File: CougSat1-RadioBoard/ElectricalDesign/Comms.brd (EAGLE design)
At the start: 90.4 x 95.8 mm, 317 parts, among them J1 700mm Antenna, J2 CougSat Card, J3 SWD, Q1 DMN53D0LDW, Q2 DMN53D0LDW, Q3 DMN53D0LDW, Q4 CSD25402Q3A, U1 AD8515, U10 AD8515, U11 AD8515, U12 TXS0102DQM, U13 ADF4360, U14 MAAM-011229, U15 INA199C2, U16 AD8515, U17 AD8515, U18 LP5907MFX-3.1, U19 HMC545A, U2 AD8515, U20 INA199C1, U21 TPS61236, U22 AD8345, U23 AD9761, U24 TXS0102DQM, U25 TXS0102DQM, U26 TXS0102DQM, U27 MMZ09332B, U28 AD8515, U29 ADF4360, U3 AD7291, U30 TXS0102DQM, U31 INA199C2, U32 TXS0102DQM, U33 LP5907MFX-3.1, U34 MAAM-011229, U35 TXS0102DQM, U36 TXS0102DQM, U37 STM32L496VGT, U38 IS25LP016D, U39 IS25LP016D, U4 AD7291, U5 MAAM-011229, U6 AD8348, U7 AD7291, U8 MAAM-011229, U9 TXS0102DQM, Y1 19.68MHz ±2.5ppm, Y2 19.68MHz ±2.5ppm, Y3 8MHz ±10ppm, Y4 32.768kHz ±10ppm

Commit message: Adjusted layout
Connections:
- net SELFNET renamed PA_HEATSINK
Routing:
- net PA_HEATSINK: track 0.00 -> 4.53 mm, vias 0 -> 7
- net DGND: track 2435.8 -> 2435.7 mm, vias 949 -> 944
- added copper zone on layer 15, net PA_HEATSINK
- added copper zone on layer 16, net PA_HEATSINK
- added copper zone on layer 2, net PA_HEATSINK
- removed copper zone on layer 16, net HEAT1
- removed copper zone on layer 15, net HEAT2
- removed copper zone on layer 2, net HEAT3
- removed copper zone on layer 1, net HEAT4
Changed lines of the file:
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@@
 <drawing>
 <settings>
-<setting alwaysvectorfont="no"/>
+<setting alwaysvectorfont="yes"/>
 <setting verticaltext="up"/>
 </settings>
@@
 <layer number="28" name="bValues" color="7" fill="1" visible="no" active="yes"/>
 <layer number="29" name="tStop" color="7" fill="3" visible="no" active="yes"/>
-<layer number="30" name="bStop" color="7" fill="6" visible="no" active="yes"/>
+<layer number="30" name="bStop" color="7" fill="6" visible="yes" active="yes"/>
 <layer number="31" name="tCream" color="7" fill="4" visible="no" active="yes"/>
 <layer number="32" name="bCream" color="7" fill="5" visible="no" active="yes"/>
@@
 <circle x="76.25" y="4.9" radius="0.3" width="0" layer="30"/>
 <circle x="76.25" y="3.5" radius="0.3" width="0" layer="30"/>
-<circle x="77.9" y="-3.4" radius="0.3" width="0" layer="30"/>
-<circle x="77.4" y="-2.9" radius="0.3" width="0" layer="30"/>
-<circle x="78.4" y="-2.9" radius="0.3" width="0" layer="30"/>
-<circle x="78.4" y="-3.9" radius="0.3" width="0" layer="30"/>
-<circle x="77.4" y="-3.9" radius="0.3" width="0" layer="30"/>
 <circle x="80" y="-3.4" radius="0.3" width="0" layer="30"/>
 <circle x="80" y="-4" radius="0.3" width="0" layer="30"/>
@@
 <circle x="78.7" y="0" radius="0.3" width="0" layer="30"/>
 <circle x="77.25" y="0.4" radius="0.3" width="0" layer="30"/>
-<circle x="76.5" y="-1.9" radius="0.3" width="0" layer="30"/>
 <circle x="79.3" y="-1.9" radius="0.3" width="0" layer="30"/>
 <circle x="79" y="2" radius="0.3" width="0" layer="30"/>
@@
 <circle x="37.6" y="34.85" radius="0.3" width="0" layer="30"/>
 <circle x="31.22" y="32.55" radius="0.3" width="0" layer="30"/>
+<polygon width="0.2" layer="30">
+<vertex x="76.1" y="-3.1"/>
+<vertex x="76.1" y="-1.5"/>
+<vertex x="76.2" y="-1.4"/>
+<vertex x="78.1" y="-1.4"/>
+<vertex x="79.4" y="-2.7"/>
+<vertex x="79.4" y="-4.2"/>
+<vertex x="77.2" y="-4.2"/>
+</polygon>
 </plain>
 <attributes>
@@
 <via x="76.25" y="4.9" extent="1-16" drill="0.3"/>
 <via x="76.25" y="3.5" extent="1-16" drill="0.3"/>
-<via x="77.9" y="-3.4" extent="1-16" drill="0.3"/>
-<via x="77.4" y="-2.9" extent="1-16" drill="0.3"/>
-<via x="78.4" y="-2.9" extent="1-16" drill="0.3"/>
-<via x="78.4" y="-3.9" extent="1-16" drill="0.3"/>
-<via x="77.4" y="-3.9" extent="1-16" drill="0.3"/>
 <via x="80" y="-3.4" extent="1-16" drill="0.3"/>
 <via x="80" y="-4" extent="1-16" drill="0.3"/>
@@
 </polygon>
 <polygon width="0.2" layer="15" thermals="no">
-<vertex x="77.3" y="-2.7"/>
-<vertex x="77.2" y="-2.8"/>
-<vertex x="77.2" y="-4"/>
-<vertex x="77.3" y="-4.1"/>
-<vertex x="78.5" y="-4.1"/>
-<vertex x="78.6" y="-4"/>
-<vertex x="78.6" y="-2.8"/>
-<vertex x="78.5" y="-2.7"/>
-</polygon>
-<polygon width="0.2" layer="15" thermals="no">
 <vertex x="79.9" y="-3.2"/>
 <vertex x="79.8" y="-3.3"/>
@@
 <wire x1="71" y1="1" x2="73.1" y2="-1.1" width="0.25" layer="2"/>
 <wire x1="73.1" y1="-1.1" x2="73.1" y2="-1.25" width="0.25" layer="2"/>
-<wire x1="79.3" y1="-2" x2="79.3" y2="-1.9" width="0.25" layer="2"/>
 <wire x1="80" y1="-3.4" x2="80" y2="-2.6" width="0.25" layer="2"/>
 <wire x1="80" y1="-2.6" x2="79.3" y2="-1.9" width="0.25" layer="2"/>
@@
 <wire x1="87.4" y1="-26.975" x2="40.175" y2="-26.975" width="0.16" layer="1"/>
 </signal>
-<signal name="SELFNET">
-<contactref element="U27" pad="PAD"/>
-</signal>
-<signal name="HEAT1">
-<polygon width="0.1524" layer="16">
-<vertex x="77.4" y="-3.8"/>
-<vertex x="76.9" y="-4.3"/>
-<vertex x="74.4" y="-4.3"/>
-<vertex x="75.1" y="-3.6"/>
-<vertex x="75.1" y="-2.2"/>
-<vertex x="76.7" y="-3.8"/>
-</polygon>
-</signal>
-<signal name="HEAT2">
-<polygon width="0.1524" layer="15">
-<vertex x="77.3" y="-2.9"/>
-<vertex x="74.5" y="-2.9"/>
-<vertex x="74.4" y="-3"/>
-<vertex x="74.4" y="-1.1"/>
-<vertex x="75.5" y="0"/>
-<vertex x="76.7" y="0"/>
-<vertex x="77.3" y="-0.6"/>
-</polygon>
-</signal>
-<signal name="HEAT4">
-<polygon width="0.1524" layer="1">
-<vertex x="78.5" y="-3.9"/>
-<vertex x="76" y="-6.4"/>
-<vertex x="76" y="-6.6"/>
-<vertex x="77.2" y="-7.8"/>
-<vertex x="79.5" y="-7.8"/>
-<vertex x="81.3" y="-7.8"/>
-<vertex x="81.8" y="-7.3"/>
-<vertex x="78.5" y="-4"/>
-</polygon>
-</signal>
-<signal name="HEAT3">
-<polygon width="0.1524" layer="2">
-<vertex x="78.4" y="-2.9"/>
-<vertex x="76.9" y="-1.4"/>
+<signal name="PA_HEATSINK">
+<polygon width="0.2" layer="2">
+<vertex x="78.6" y="-4.1"/>
+<vertex x="77.2" y="-4.1"/>
+<vertex x="77.2" y="-2.7"/>
+<vertex x="78.6" y="-2.7"/>
+</polygon>
+<polygon width="0.2" layer="15">
+<vertex x="79" y="-4.9"/>
+<vertex x="76.8" y="-4.9"/>
+<vertex x="75.9" y="-4"/>
+<vertex x="75.9" y="-1.7"/>
 <vertex x="76.2" y="-1.4"/>
-<vertex x="77.7" y="0.1"/>
-<vertex x="78" y="0.1"/>
-<vertex x="79.6" y="-1.5"/>
-<vertex x="79.6" y="-2.9"/>
+<vertex x="78.5" y="-1.4"/>
+<vertex x="79.4" y="-2.3"/>
+<vertex x="79.4" y="-4.5"/>
+</polygon>
+<polygon width="0.2" layer="16">
+<vertex x="79.4" y="-4.5"/>
+<vertex x="77.1" y="-4.5"/>
+<vertex x="75.9" y="-3.3"/>
+<vertex x="75.9" y="-1.7"/>
+<vertex x="76.2" y="-1.4"/>
+<vertex x="79.5" y="-1.4"/>
+<vertex x="79.8" y="-1.7"/>
+<vertex x="79.8" y="-4.1"/>
 </polygon>
+<contactref element="U27" pad="PAD"/>
+<via x="77.9" y="-3.4" extent="1-16" drill="0.3"/>
+<via x="78.4" y="-2.9" extent="1-16" drill="0.3"/>
+<via x="78.4" y="-3.9" extent="1-16" drill="0.3"/>
+<via x="77.4" y="-3.9" extent="1-16" drill="0.3"/>
+<via x="77.4" y="-2.9" extent="1-16" drill="0.3"/>
+<via x="76.7" y="-2.2" extent="1-16" drill="0.3"/>
+<via x="76.2" y="-1.7" extent="1-16" drill="0.3"/>
+<wire x1="76.2" y1="-1.7" x2="76.7" y2="-2.2" width="0.2" layer="15"/>
+<wire x1="76.7" y1="-2.2" x2="77.4" y2="-2.9" width="0.2" layer="15"/>
+<wire x1="77.4" y1="-2.9" x2="77.9" y2="-3.4" width="0.2" layer="15"/>
+<wire x1="77.9" y1="-3.4" x2="78.4" y2="-3.9" width="0.2" layer="15"/>
+<wire x1="78.4" y1="-2.9" x2="77.9" y2="-3.4" width="0.2" layer="15"/>
+<wire x1="77.4" y1="-3.9" x2="77.9" y2="-3.4" width="0.2" layer="15"/>
 </signal>
 </signals>

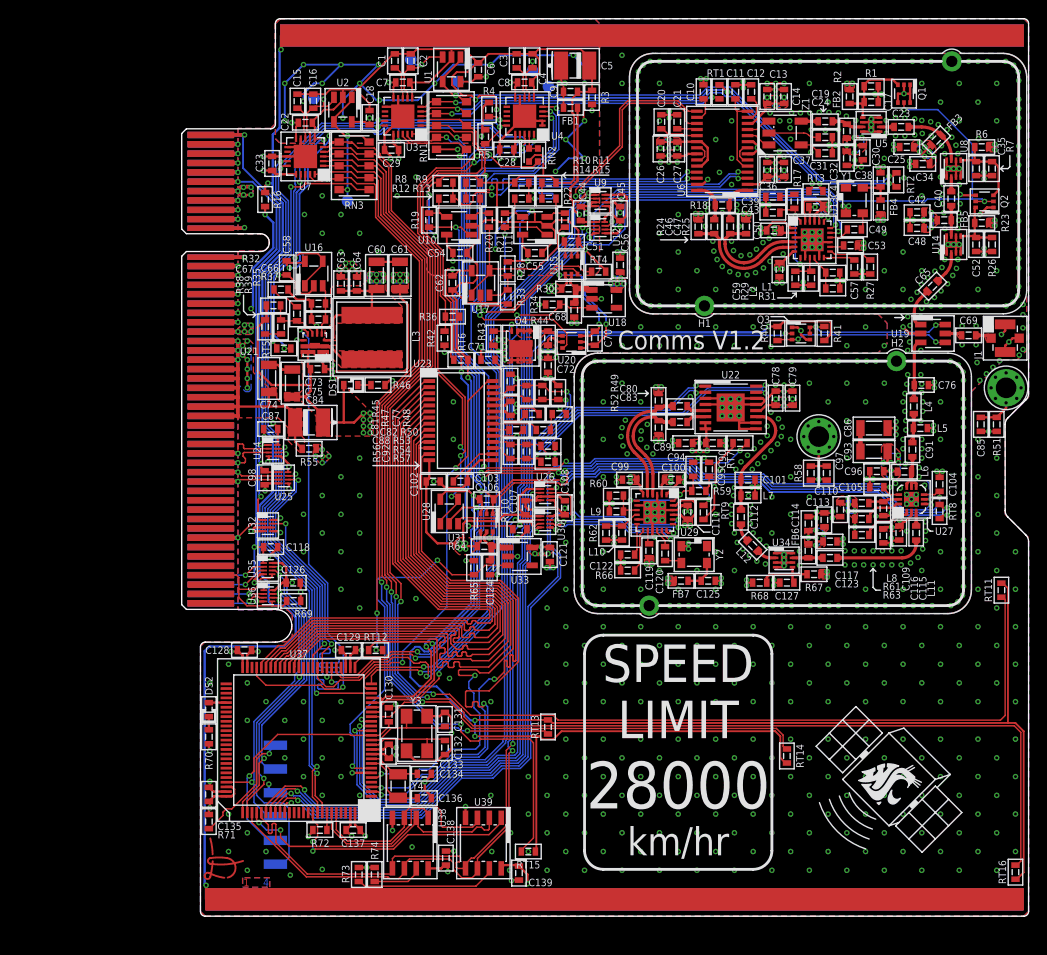
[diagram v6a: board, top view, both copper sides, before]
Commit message: Added nFET
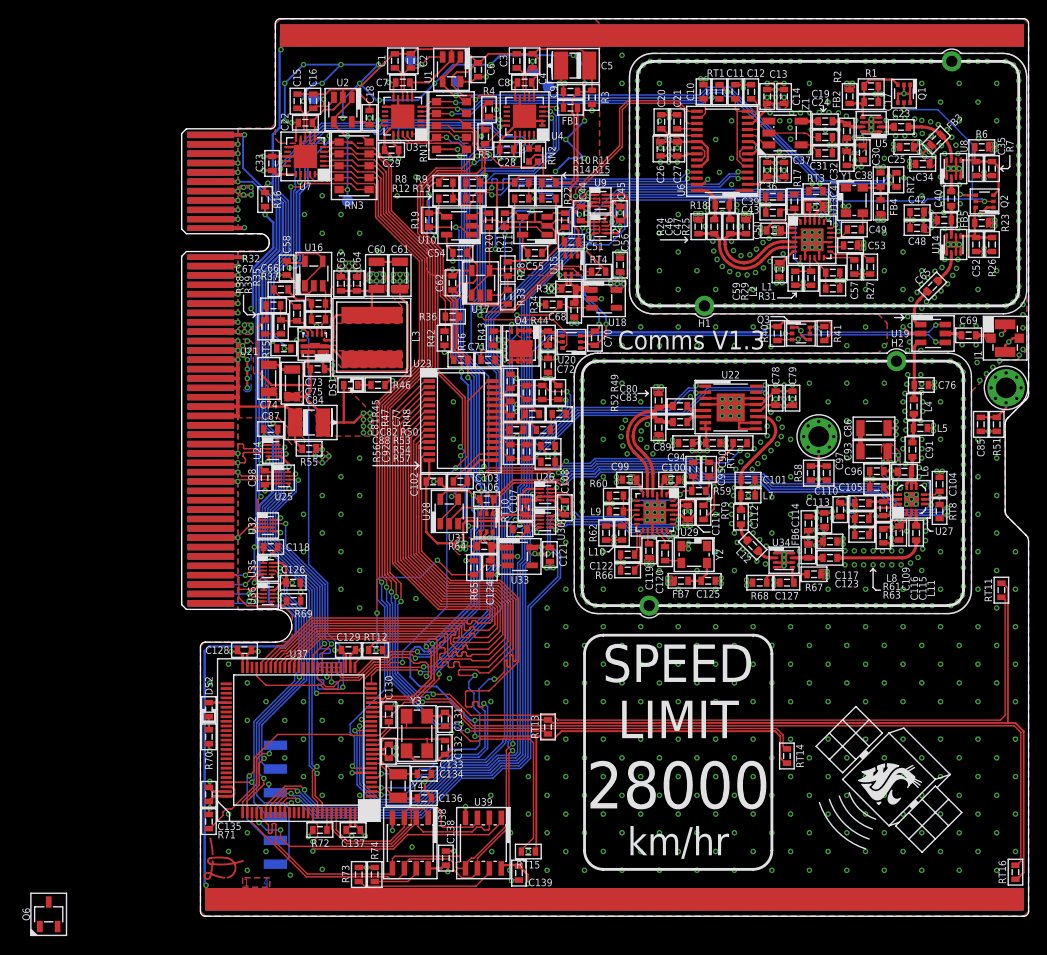
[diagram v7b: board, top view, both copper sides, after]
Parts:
- added Q6: DMN53D0L, CougsInSpace-DiscreteSemi:SOT23-3
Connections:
- new net PC_5.0: Q6.1
- net !PC_5.0V-1: now also Q6.3
- net PGND: now also Q6.2
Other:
- board text added: "Comms V1.3"
- board text removed: "Comms V1.2"
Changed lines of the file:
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@@
 <drawing>
 <settings>
-<setting alwaysvectorfont="yes"/>
+<setting alwaysvectorfont="no"/>
 <setting verticaltext="up"/>
 </settings>
@@
 <wire x1="77.1" y1="16" x2="76.8" y2="16.3" width="0.15" layer="21"/>
 <wire x1="77.1" y1="16" x2="76.8" y2="15.7" width="0.15" layer="21"/>
-<text x="54.4" y="13.6" size="2" layer="21" font="vector" ratio="15" align="center">Comms V1.2</text>
+<text x="54.4" y="13.6" size="2" layer="21" font="vector" ratio="15" align="center">Comms V1.3</text>
 <text x="6.9" y="-44.3" size="0.8" layer="1" font="vector" ratio="15" align="center">1</text>
 <text x="7.6" y="-44.3" size="0.8" layer="2" font="vector" ratio="15" align="center">2</text>
@@
 <attribute name="TEMP" value="25ppm/°C" x="6.1" y="-28.25" size="0.8" layer="27" ratio="15" rot="R90" display="off"/>
 </element>
+<element name="Q6" library="CougsInSpace-DiscreteSemi" package="SOT23-3" value="DMN53D0L" x="-14.2" y="-47.7" smashed="yes" rot="R90">
+<attribute name="CURRENT" value="500mA" x="-14.2" y="-47.7" size="1.778" layer="27" rot="R90" display="off"/>
+<attribute name="NAME" x="-16.6" y="-47.7" size="0.8" layer="25" font="vector" ratio="15" rot="R90" align="center"/>
+<attribute name="RDS" value="4.5mΩ" x="-14.2" y="-47.7" size="1.778" layer="27" rot="R90" display="off"/>
+<attribute name="SKU" value="56-0003" x="-14.2" y="-47.7" size="1.778" layer="27" rot="R90" display="off"/>
+<attribute name="VDS" value="50V" x="-14.2" y="-47.7" size="1.778" layer="27" rot="R90" display="off"/>
+</element>
 </elements>
 <signals>
@@
 <wire x1="23.3" y1="18.2" x2="24.15" y2="17.35" width="0.25" layer="1"/>
 <wire x1="24.15" y1="17.35" x2="24.15" y2="10.65" width="0.25" layer="1"/>
+<contactref element="Q6" pad="2"/>
+<wire x1="3.1" y1="5.5" x2="-13.25" y2="-49.01" width="0" layer="19" extent="1-1"/>
 </signal>
 <signal name="CHASSIS" class="3">
@@
 <wire x1="20.25" y1="-27.1" x2="19.4" y2="-27.1" width="0.16" layer="1"/>
 <wire x1="19.4" y1="-27.1" x2="19.2" y2="-26.9" width="0.16" layer="1"/>
+<contactref element="Q6" pad="3"/>
+<wire x1="19.2" y1="-26.9" x2="-14.2" y2="-46.39" width="0" layer="19" extent="1-1"/>
 </signal>
 <signal name="I_5.0V-1">
@@
 <wire x1="77.4" y1="-3.9" x2="77.9" y2="-3.4" width="0.2" layer="15"/>
 </signal>
+<signal name="PC_5.0">
+<contactref element="Q6" pad="1"/>
+</signal>
 </signals>

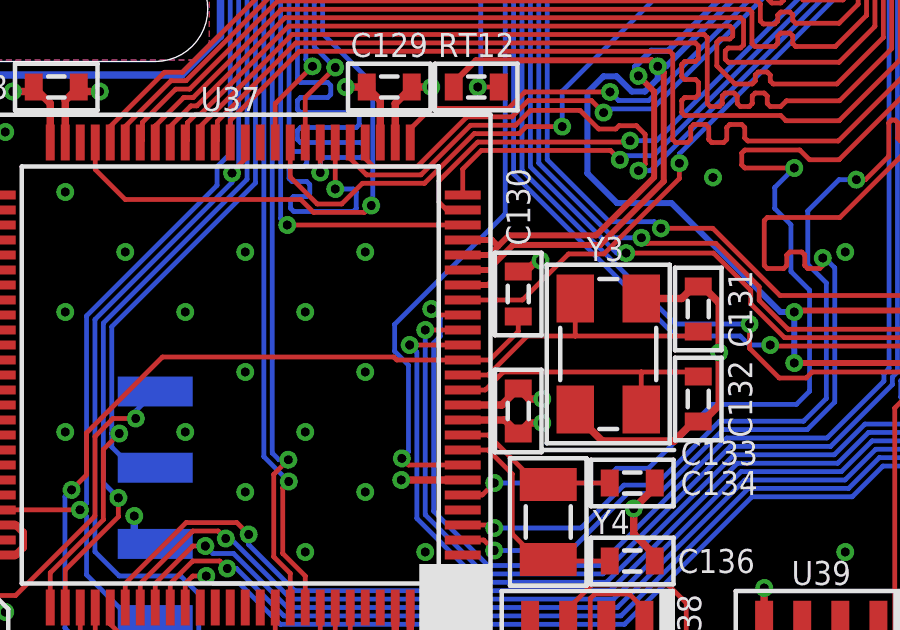
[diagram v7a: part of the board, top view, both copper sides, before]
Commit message: Fixed net names
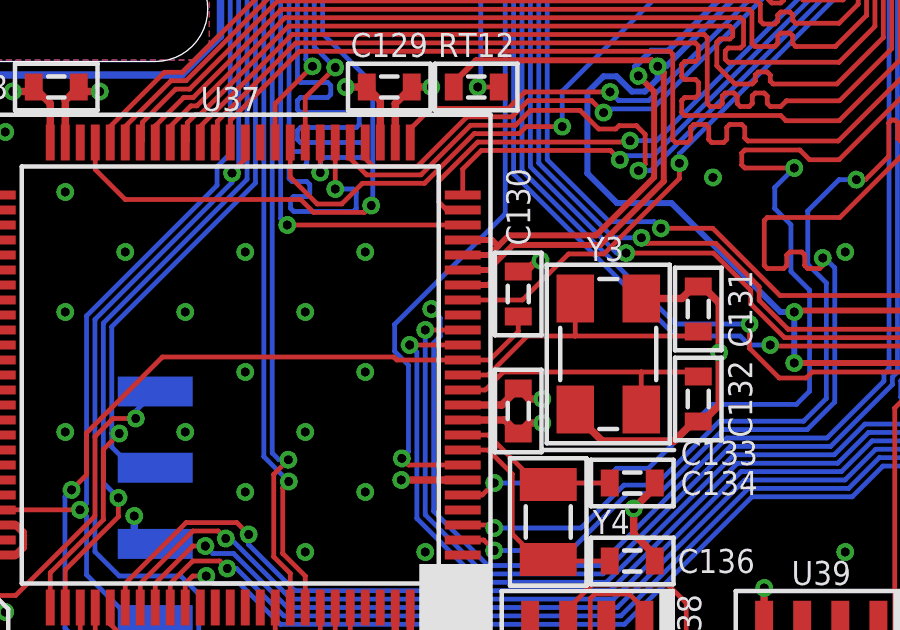
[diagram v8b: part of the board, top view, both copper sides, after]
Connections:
- removed net !PC_5.0V-1: Q4.4, Q6.3, R43.1, U37.17
- removed net PC_5.0: Q6.1
- new net !PC_5.0V: Q4.4, Q6.3, R43.1
- new net PC_5.0V: Q6.1, U37.17
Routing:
- net !PC_5.0V-1: track 74.0 -> 0.00 mm, vias 2 -> 0
- net !PC_5.0V: track 0.00 -> 73.1 mm, vias 0 -> 2
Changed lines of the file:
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@@
 <wire x1="21.13" y1="-11.74" x2="25.46" y2="-11.74" width="0.16" layer="16"/>
 </signal>
-<signal name="!PC_5.0V-1">
+<signal name="!PC_5.0V">
 <contactref element="Q4" pad="4"/>
 <contactref element="R43" pad="1"/>
@@
 <wire x1="19.28" y1="-28.03" x2="19.5" y2="-27.81" width="0.16" layer="16"/>
 <wire x1="19.5" y1="-27.81" x2="19.5" y2="-27.2" width="0.16" layer="16"/>
-<contactref element="U37" pad="17"/>
-<wire x1="20.25" y1="-27.1" x2="19.4" y2="-27.1" width="0.16" layer="1"/>
 <wire x1="19.4" y1="-27.1" x2="19.2" y2="-26.9" width="0.16" layer="1"/>
 <contactref element="Q6" pad="3"/>
@@
 <wire x1="77.4" y1="-3.9" x2="77.9" y2="-3.4" width="0.2" layer="15"/>
 </signal>
-<signal name="PC_5.0">
+<signal name="PC_5.0V">
+<contactref element="U37" pad="17"/>
 <contactref element="Q6" pad="1"/>
+<wire x1="20.25" y1="-27.1" x2="-15.15" y2="-49.01" width="0" layer="19" extent="1-1"/>
 </signal>
 </signals>
